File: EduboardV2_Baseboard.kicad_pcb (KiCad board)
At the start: 2 copper layers, 100 x 160 mm, 145 parts, among them IC201 STK8321, IC202 PCF8563T_5,518, IC203 W25Q128JVSIQTR, IC301 XL1509-5.0E1, IC302 SY8113BADC, IC601 STK8321, IC602 SP3485EN-L_TR, IC603 WM8782SEDS_RV_C323842, IC604 CS4344-CZZ, IC605 MCP9700AT-E_TT, SW301 1FS1T1B9M2RES-5, SW401 K2-1102SP-C4SC-04, SW402 K2-1102SP-C4SC-04, SW403 K2-1102SP-C4SC-04, SW404 K2-1102SP-C4SC-04, T401 AO3400A, T402 AO3400A, T403 AO3400A, T404 AO3400A, T405 AO3400A, X201 PCIE-52P40H, X202 32.768 kHz, X203 TF-15×15, X301 KF2EDGR-3.81-3P, X302 USB3.1C16PFSMT, X303 CH340G, X401 ER-TFT035-6, X501 BH-00105, X502 S4B-PH-SM4-K-TB(LF)(SN), X503 USB3.1C16PFSMT, X601 KF2EDGR-3.81-3P, X602 PJ-327C-4A, X603 PJ-327C-4A, Y301 X322512MSB4SI

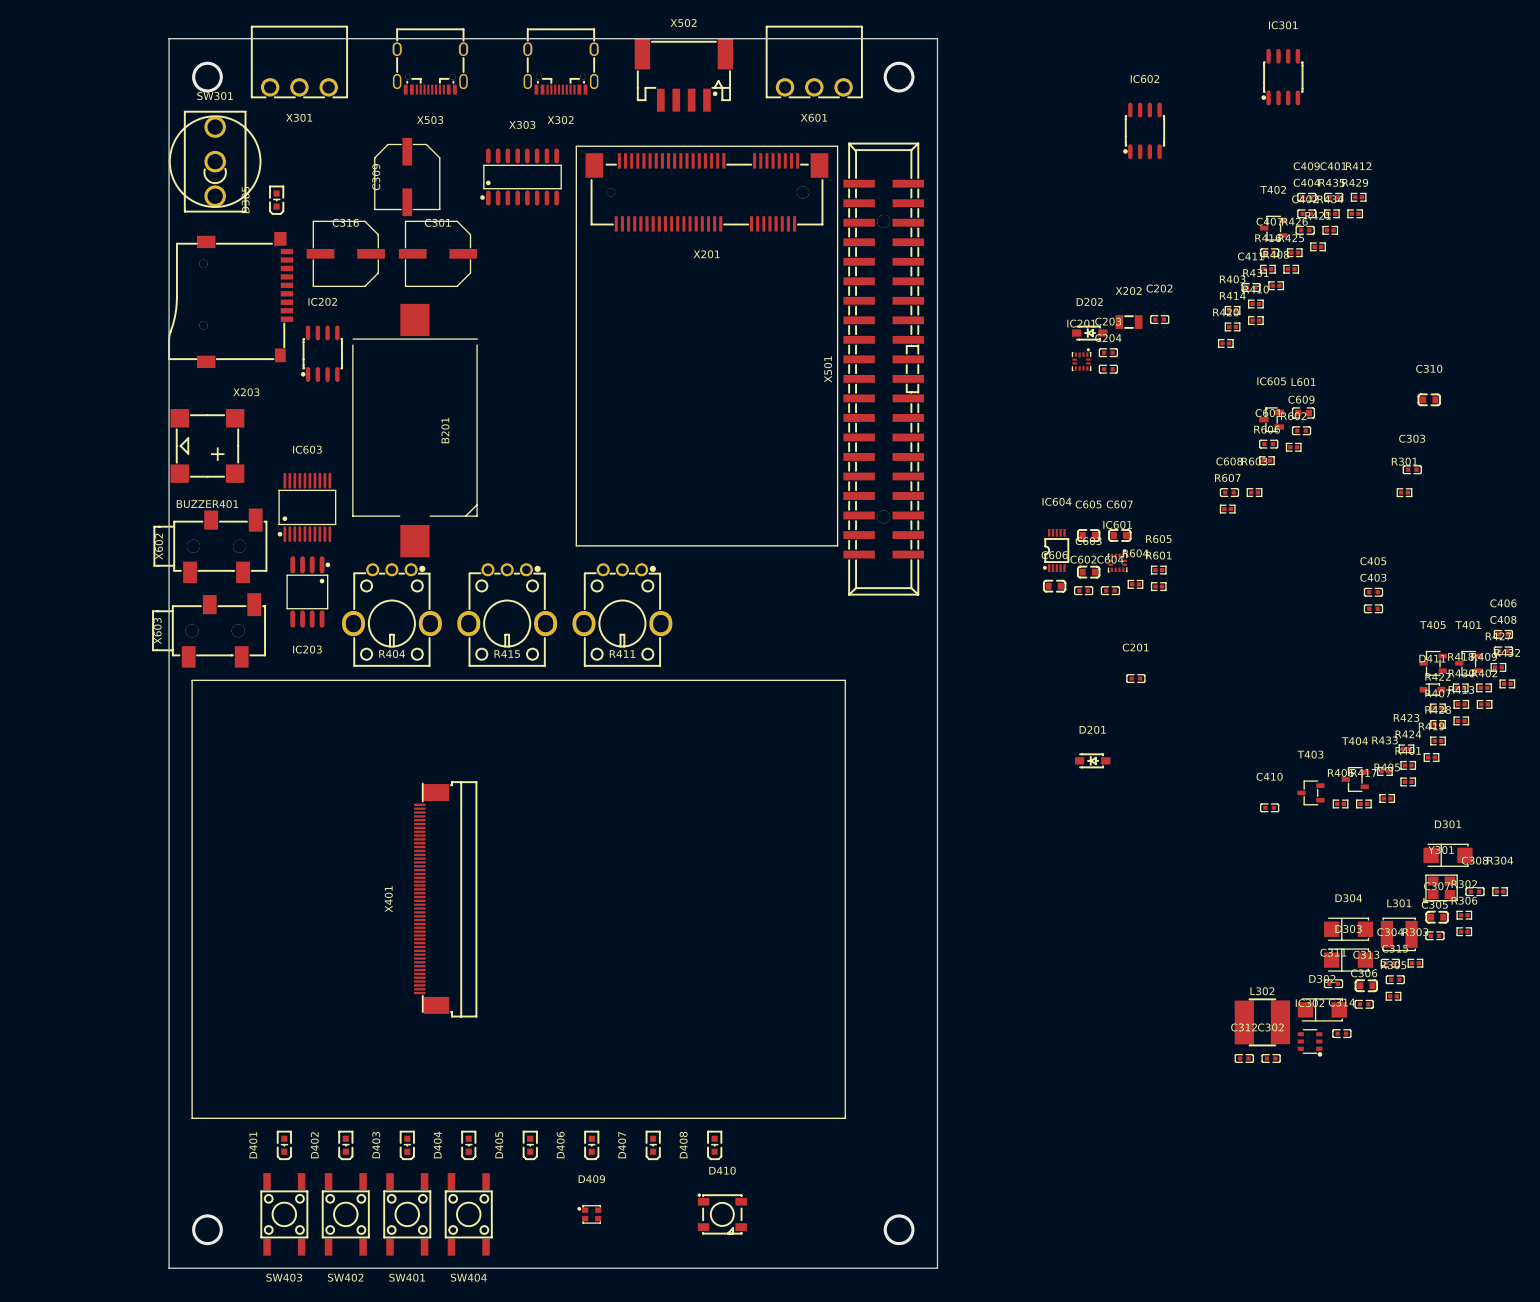
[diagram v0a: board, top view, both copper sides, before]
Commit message: positioned components. Exchanged battery holder
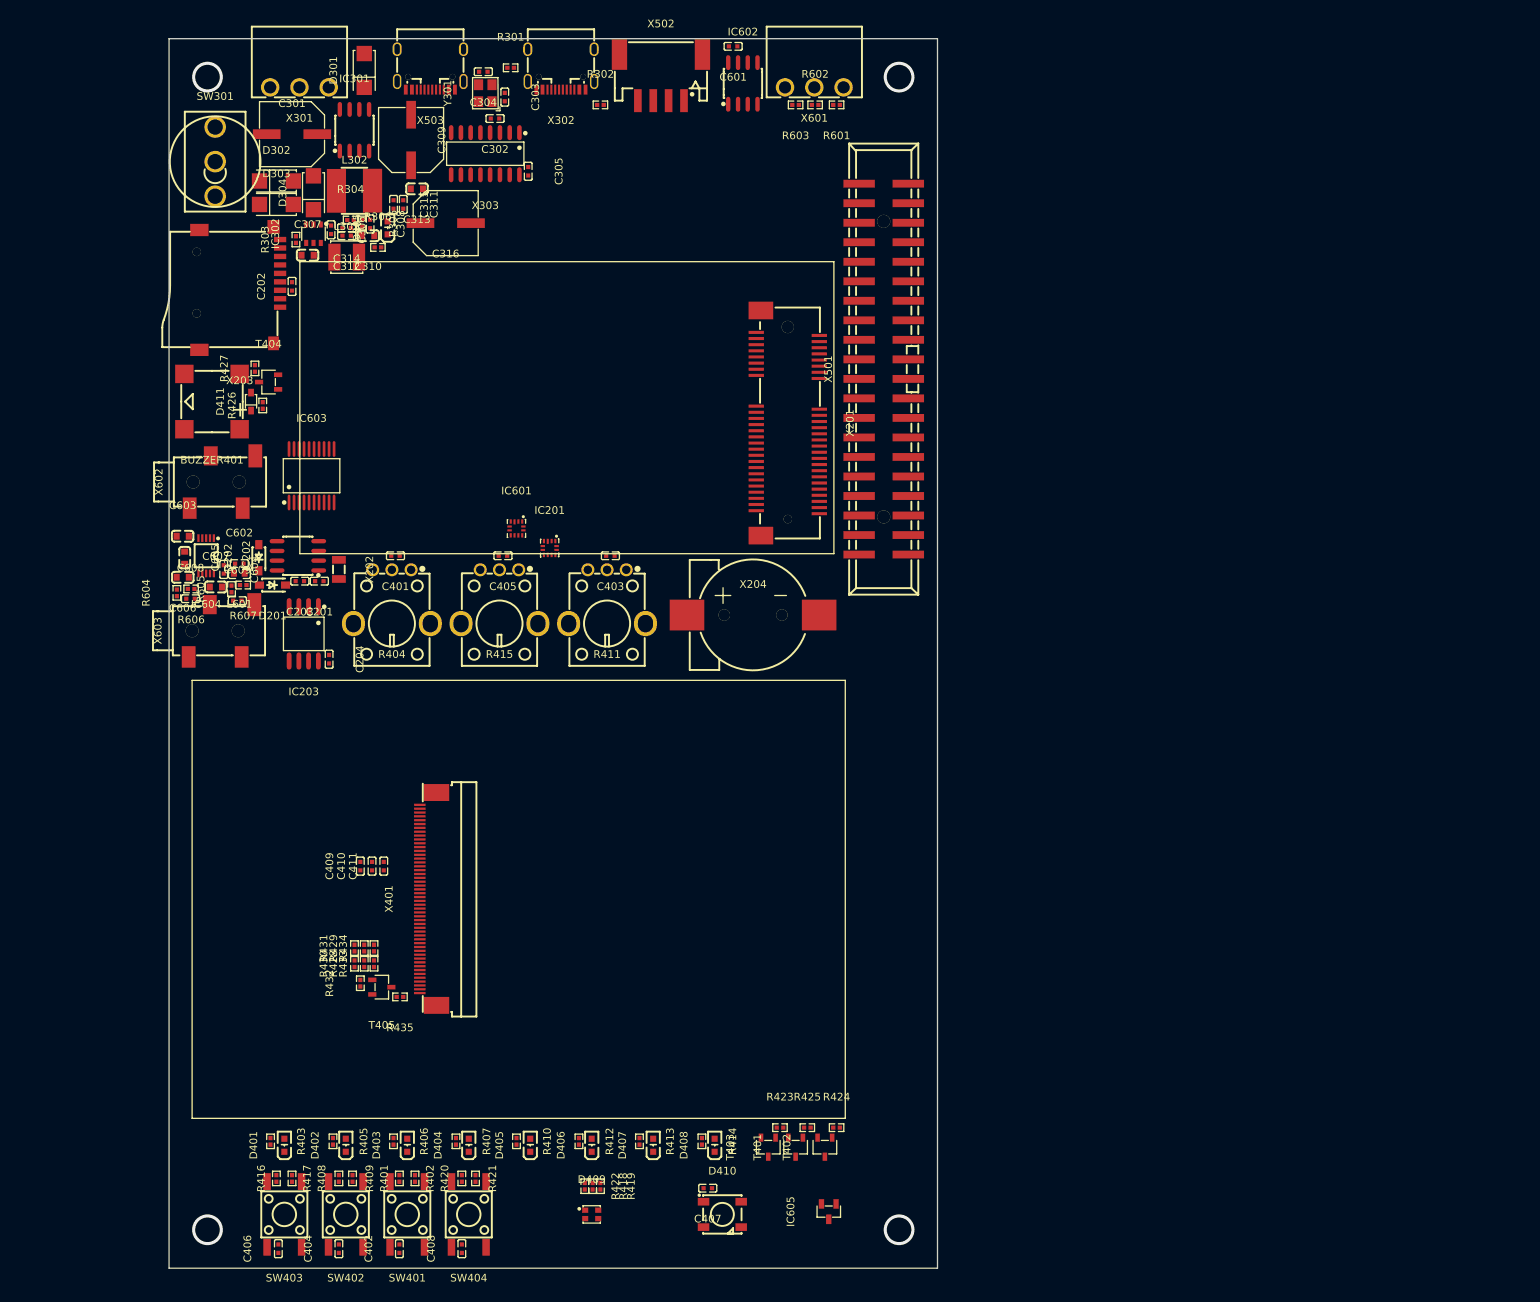
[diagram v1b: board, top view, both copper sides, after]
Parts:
- removed B201: CR2032-BS-6-1, eduboardv2:BAT-TH_CR2032-BS-6-1
- added X204: CR1220-2ZX, eduboardv2:BAT-SMD_CR1220-2ZX, F.Cu at (130.0, 96.0)
- moved C404 184.4 mm to (76.1, 178.5), turned to 90 degrees
- moved C406 178.3 mm to (68.2, 178.5), turned to 90 degrees
- moved C402 177.4 mm to (84.0, 178.5), turned to 90 degrees
- moved D301 174.1 mm to (79.4, 25.1), turned to 90 degrees
- moved D302 173.7 mm to (68.0, 39.5)
- moved R416 173.6 mm to (70.0, 169.3), turned to 90 degrees
- moved R303 173.5 mm to (70.5, 47.1), turned to 90 degrees
- moved R304 173.2 mm to (77.6, 44.6)
- moved D303 170.7 mm to (68.0, 42.6)
- moved C307 170.4 mm to (72.0, 49.2)
- moved C306 168.0 mm to (75.1, 45.9), turned to -90 degrees
- moved C308 168.0 mm to (80.2, 45.1), turned to -90 degrees
- moved R305 167.7 mm to (79.1, 45.0), turned to -90 degrees
- moved R408 167.2 mm to (77.9, 169.3), turned to 90 degrees
- moved R306 167.1 mm to (81.2, 48.2)
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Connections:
- net /Connectors/USB1_D+ renamed USB1_D+
- net /Connectors/USB1_D- renamed USB1_D-
- net /Display_and_UI/AN0 renamed AN0
- net /Display_and_UI/AN1 renamed AN1
- net /Display_and_UI/AN2 renamed AN2
- net /Display_and_UI/BUZZER renamed BUZZER
- net /Display_and_UI/LED0 renamed LED0
- net /Display_and_UI/LED1 renamed LED1
- net /Display_and_UI/LED2 renamed LED2
- net /Display_and_UI/LED3 renamed LED3
- net /Display_and_UI/LED4 renamed LED4
- net /Display_and_UI/LED5 renamed LED5
- net /Display_and_UI/LED6 renamed LED6
- net /Display_and_UI/LED7 renamed LED7
- net /Display_and_UI/PWMB renamed PWMB
- net /Display_and_UI/PWMG renamed PWMG
- net /Display_and_UI/PWMR renamed PWMR
- net /Display_and_UI/SW0 renamed SW0
- net /Display_and_UI/SW1 renamed SW1
- net /Display_and_UI/TFT_BKL renamed TFT_BKL
- net /Display_and_UI/TFT_CS renamed TFT_CS
- net /Display_and_UI/TFT_DCX renamed TFT_DCX
- net /Display_and_UI/TFT_RST renamed TFT_RST
- net /Display_and_UI/TFT_SCL renamed TFT_SCL
- net /Display_and_UI/TFT_SDA renamed TFT_SDA
- net /Display_and_UI/TFT_SDO renamed TFT_SDO
- net /Display_and_UI/TFT_TE renamed TFT_TE
- net /Display_and_UI/TFT_TP_IRQ renamed TFT_TP_IRQ
- net /Display_and_UI/TFT_TP_RST renamed TFT_TP_RST
- net /Display_and_UI/TFT_TP_SCL renamed TFT_TP_SCL
- net /Display_and_UI/TFT_TP_SDA renamed TFT_TP_SDA
- net /Display_and_UI/WS2812_DIN renamed WS2812_DIN
- net /Power/USB0_D+ renamed USB0_D+
- net /Power/USB0_D- renamed USB0_D-
- net /Power/USB_UART0_RX renamed USB_UART0_RX
- net /Power/USB_UART0_TX renamed USB_UART0_TX
- net /Sensors and Interfaces/I2S0_LRCK renamed I2S0_LRCK
- net /Sensors and Interfaces/I2S0_MCLK renamed I2S0_MCLK
- net /Sensors and Interfaces/I2S0_SCLK renamed I2S0_SCLK
- net /Sensors and Interfaces/I2S0_SDIN renamed I2S0_SDIN
- net /Sensors and Interfaces/RS485_DE renamed RS485_DE
- net /Sensors and Interfaces/UART_RS485_RX renamed UART_RS485_RX
- net /Sensors and Interfaces/UART_RS485_TX renamed UART_RS485_TX
- net /UP-Connector, RTC and Flash/FLASH_CS renamed FLASH_CS
- net /UP-Connector, RTC and Flash/RTC_CLK renamed RTC_CLK
- net /UP-Connector, RTC and Flash/RTC_INT renamed RTC_INT
- net /UP-Connector, RTC and Flash/SCL0 renamed SCL0
- net /UP-Connector, RTC and Flash/SDA0 renamed SDA0
- net /UP-Connector, RTC and Flash/SDCARD_CS renamed SDCARD_CS
- net /UP-Connector, RTC and Flash/SPI0_CLK renamed SPI0_CLK
- net /UP-Connector, RTC and Flash/SPI0_MISO renamed SPI0_MISO
- net /UP-Connector, RTC and Flash/SPI0_MOSI renamed SPI0_MOSI
- BUZZER401 pad 1: +3.3V -> Net-(BUZZER401-Pad1)
- C201 pad 2: GND -> Net-(C201-Pad2)
- C202 pad 1: GND -> Net-(C202-Pad1)
- C202 pad 2: +3.3V -> Net-(C202-Pad2)
- C203 pad 1: GND -> Net-(C203-Pad1)
- C204 pad 1: GND -> Net-(C204-Pad1)
- C204 pad 2: +3.3V -> Net-(C204-Pad2)
- C301 pad 1: V_EXT -> Net-(C301-Pad1)
- C301 pad 2: GND -> Net-(C301-Pad2)
- C302 pad 1: GND -> Net-(C302-Pad1)
- C303 pad 1: GND -> Net-(C303-Pad1)
- C304 pad 1: GND -> Net-(C304-Pad1)
- C305 pad 1: GND -> Net-(C305-Pad1)
- C305 pad 2: V_USB -> Net-(C305-Pad2)
- C307 pad 1: GND -> Net-(C307-Pad1)
- C307 pad 2: +5V -> Net-(C307-Pad2)
- C308 pad 2: +3.3V -> Net-(C308-Pad2)
- C309 pad 1: +5V_EXT -> Net-(C309-Pad1)
- C309 pad 2: GND -> Net-(C309-Pad2)
- C310 pad 1: GND -> Net-(C310-Pad1)
- C310 pad 2: +3.3V -> Net-(C308-Pad2)
- C311 pad 1: +5V_EXT -> Net-(C309-Pad1)
- C311 pad 2: GND -> Net-(C311-Pad2)
- C312 pad 1: +3.3V -> Net-(C308-Pad2)
- C312 pad 2: GND -> Net-(C312-Pad2)
- C313 pad 1: GND -> Net-(C313-Pad1)
- C313 pad 2: +5V_EXT -> Net-(C309-Pad1)
- C314 pad 1: +3.3V -> Net-(C308-Pad2)
- C314 pad 2: GND -> Net-(C314-Pad2)
- C315 pad 1: +5V_EXT -> Net-(C309-Pad1)
- C315 pad 2: GND -> Net-(C315-Pad2)
- C316 pad 1: +3.3V -> Net-(C308-Pad2)
- C316 pad 2: GND -> Net-(C316-Pad2)
- C401 pad 1: GND -> Net-(C401-Pad1)
- C402 pad 1: GND -> Net-(C402-Pad1)
- C403 pad 1: GND -> Net-(C403-Pad1)
- C404 pad 1: GND -> Net-(C404-Pad1)
- C405 pad 1: GND -> Net-(C405-Pad1)
- C406 pad 1: GND -> Net-(C406-Pad1)
- C406 pad 2: /Display_and_UI/SW2 -> SW2
- C407 pad 1: GND -> Net-(C407-Pad1)
- C408 pad 1: GND -> Net-(C408-Pad1)
- C408 pad 2: /Display_and_UI/SW3 -> SW2
- C409 pad 1: GND -> Net-(C409-Pad1)
- C409 pad 2: +3.3V -> Net-(C409-Pad2)
- C410 pad 1: GND -> Net-(C409-Pad1)
- C410 pad 2: +3.3V -> Net-(C409-Pad2)
- C411 pad 1: GND -> Net-(C409-Pad1)
- C411 pad 2: +3.3V -> Net-(C409-Pad2)
- C601 pad 1: GND -> Net-(C601-Pad1)
- C601 pad 2: +3.3V -> Net-(C601-Pad2)
- C602 pad 1: GND -> Net-(C602-Pad1)
- C602 pad 2: +3.3V -> Net-(C602-Pad2)
- C603 pad 1: GND -> Net-(C603-Pad1)
- C604 pad 1: GND -> Net-(C604-Pad1)
- C605 pad 1: GND -> Net-(C605-Pad1)
- C608 pad 1: GND -> Net-(C608-Pad1)
- C609 pad 1: GND -> Net-(C609-Pad1)
- D201 pad 2: +3.3V -> Net-(D201-Pad2)
- D301 pad 1: V_EXT -> Net-(C301-Pad1)
- D301 pad 2: GND -> Net-(D301-Pad2)
- D302 pad 2: V_USB -> Net-(D302-Pad2)
- D303 pad 2: +5V_EXT -> Net-(D303-Pad2)
- D304 pad 2: GND -> Net-(D304-Pad2)
- D305 pad 1: +3.3V -> Net-(C308-Pad2)
- D401 pad 2: GND -> Net-(D401-Pad2)
- D402 pad 2: GND -> Net-(D402-Pad2)
- D403 pad 2: GND -> Net-(D403-Pad2)
- D404 pad 2: GND -> Net-(D404-Pad2)
- D405 pad 2: GND -> Net-(D405-Pad2)
- D406 pad 2: GND -> Net-(D406-Pad2)
- D407 pad 2: GND -> Net-(D407-Pad2)
- D408 pad 2: GND -> Net-(D408-Pad2)
- D409 pad 3: +3.3V -> Net-(D409-Pad3)
- D410 pad 3: GND -> Net-(D410-Pad3)
- D411 pad 1: +3.3V -> Net-(BUZZER401-Pad1)
- IC202 pad 4: GND -> Net-(IC202-Pad4)
- IC203 pad 4: GND -> Net-(IC203-Pad4)
- IC203 pad 8: +3.3V -> Net-(C204-Pad2)
- IC301 pad 1: V_EXT -> Net-(IC301-Pad1)
- IC301 pad 3: +5V_EXT -> Net-(C309-Pad1)
- IC301 pad 5: GND -> Net-(IC301-Pad5)
- IC301 pad 6: GND -> Net-(IC301-Pad5)
- IC301 pad 7: GND -> Net-(IC301-Pad5)
- IC301 pad 8: GND -> Net-(IC301-Pad5)
- IC302 pad 2: GND -> Net-(IC302-Pad2)
- IC302 pad 5: +5V -> Net-(C307-Pad2)
- IC602 pad 5: GND -> Net-(IC602-Pad5)
- IC602 pad 8: +3.3V -> Net-(C601-Pad2)
- IC604 pad 8: GND -> Net-(IC604-Pad8)
- L301 pad 2: +3.3V -> Net-(C308-Pad2)
- L302 pad 2: +5V_EXT -> Net-(C309-Pad1)
- L601 pad 1: +3.3V -> Net-(C602-Pad2)
- R301 pad 2: GND -> Net-(R301-Pad2)
- R302 pad 1: GND -> Net-(R302-Pad1)
- R303 pad 2: +5V -> Net-(C307-Pad2)
- R304 pad 1: GND -> Net-(R304-Pad1)
- R305 pad 2: +3.3V -> Net-(C308-Pad2)
- R306 pad 1: GND -> Net-(R306-Pad1)
- R401 pad 2: +3.3V -> Net-(R401-Pad2)
- R402 pad 1: GND -> Net-(R402-Pad1)
- R404 pad 1: GND -> Net-(R404-Pad1)
- R404 pad 3: +3.3V -> Net-(R404-Pad3)
- R408 pad 2: +3.3V -> Net-(R408-Pad2)
- R409 pad 1: GND -> Net-(R409-Pad1)
- R411 pad 1: GND -> Net-(R411-Pad1)
- R411 pad 3: +3.3V -> Net-(R411-Pad3)
- R415 pad 1: GND -> Net-(R415-Pad1)
- R415 pad 3: +3.3V -> Net-(R415-Pad3)
- R416 pad 2: +3.3V -> Net-(R416-Pad2)
- R417 pad 1: GND -> Net-(R417-Pad1)
- R420 pad 2: +3.3V -> Net-(R420-Pad2)
- R421 pad 1: GND -> Net-(R421-Pad1)
- R428 pad 1: +3.3V -> Net-(R428-Pad1)
- R429 pad 2: GND -> Net-(R429-Pad2)
- R430 pad 1: +3.3V -> Net-(R428-Pad1)
- R431 pad 2: GND -> Net-(R429-Pad2)
- R433 pad 1: +3.3V -> Net-(R428-Pad1)
- R434 pad 2: GND -> Net-(R429-Pad2)
- R435 pad 2: +3.3V -> Net-(R435-Pad2)
- R601 pad 1: GND -> Net-(R601-Pad1)
- R603 pad 2: +3.3V -> Net-(R603-Pad2)
- R604 pad 1: GND -> Net-(R604-Pad1)
- R605 pad 1: GND -> Net-(R605-Pad1)
- SW301 pad 2: +5V -> Net-(SW301-Pad2)
- SW301 pad 3: +5V -> Net-(SW301-Pad2)
- SW403 pad 4: /Display_and_UI/SW2 -> SW2
- SW404 pad 4: /Display_and_UI/SW3 -> SW2
- T401 pad 2: GND -> Net-(T401-Pad2)
- T402 pad 2: GND -> Net-(T402-Pad2)
- T403 pad 2: GND -> Net-(T403-Pad2)
- T404 pad 2: GND -> Net-(T404-Pad2)
- T405 pad 2: GND -> Net-(T405-Pad2)
- X203 pad 4: +3.3V -> Net-(C202-Pad2)
- X203 pad 6: GND -> Net-(X203-Pad6)
- X301 pad 1: V_EXT -> Net-(C301-Pad1)
- X301 pad 3: GND -> Net-(D301-Pad2)
- X302 pad 0: GND -> Net-(X302-Pad0)
- X302 pad A1: GND -> Net-(X302-PadA1)
- X302 pad A12: GND -> Net-(X302-PadA12)
- X302 pad A4: V_USB -> Net-(R302-Pad2)
- X302 pad A9: V_USB -> Net-(R302-Pad2)
- X303 pad 1: GND -> Net-(X303-Pad1)
- X303 pad 16: V_USB -> Net-(C305-Pad2)
- X401 pad 11: GND -> Net-(X401-Pad11)
- X401 pad 12: GND -> Net-(X401-Pad11)
- X401 pad 13: +3.3V -> Net-(X401-Pad13)
- X401 pad 14: GND -> Net-(X401-Pad14)
- X401 pad 15: GND -> Net-(X401-Pad14)
- X401 pad 16: GND -> Net-(X401-Pad14)
- X401 pad 17: GND -> Net-(X401-Pad14)
- X401 pad 18: GND -> Net-(X401-Pad14)
- X401 pad 19: GND -> Net-(X401-Pad14)
- X401 pad 20: GND -> Net-(X401-Pad14)
- X401 pad 21: GND -> Net-(X401-Pad14)
- X401 pad 22: GND -> Net-(X401-Pad14)
- X401 pad 23: GND -> Net-(X401-Pad14)
- X401 pad 24: GND -> Net-(X401-Pad14)
- X401 pad 25: GND -> Net-(X401-Pad14)
- X401 pad 26: GND -> Net-(X401-Pad14)
- X401 pad 27: GND -> Net-(X401-Pad14)
- X401 pad 28: GND -> Net-(X401-Pad14)
- X401 pad 29: GND -> Net-(X401-Pad14)
- X401 pad 30: GND -> Net-(X401-Pad14)
- X401 pad 31: GND -> Net-(X401-Pad14)
- X401 pad 32: GND -> Net-(X401-Pad14)
- X401 pad 35: +3.3V -> Net-(X401-Pad35)
- X401 pad 40: +3.3V -> Net-(X401-Pad40)
- X401 pad 41: +3.3V -> Net-(X401-Pad40)
- X401 pad 42: +3.3V -> Net-(X401-Pad40)
- X401 pad 43: GND -> Net-(X401-Pad43)
- X401 pad 48: GND -> Net-(X401-Pad48)
- X401 pad 49: GND -> Net-(X401-Pad48)
- X401 pad 50: GND -> Net-(X401-Pad48)
- X503 pad 0: GND -> Net-(X503-Pad0)
- X503 pad A1: GND -> Net-(X503-PadA1)
- X503 pad A12: GND -> Net-(X503-PadA12)
- X601 pad 2: GND -> Net-(X601-Pad2)
- X603 pad 1: GND -> Net-(X603-Pad1)
- Y301 pad 2: GND -> Net-(Y301-Pad2)
- Y301 pad 4: GND -> Net-(Y301-Pad4)
